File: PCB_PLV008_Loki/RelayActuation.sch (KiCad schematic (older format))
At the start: 27 parts, among them J27 Conn_01x02, J28 Conn_01x02, J29 Conn_01x02, J30 Conn_01x01, J31 Conn_01x01, J32 Conn_01x01, J33 Conn_01x01, J34 Conn_01x02, J35 Conn_01x02, J36 Conn_01x01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

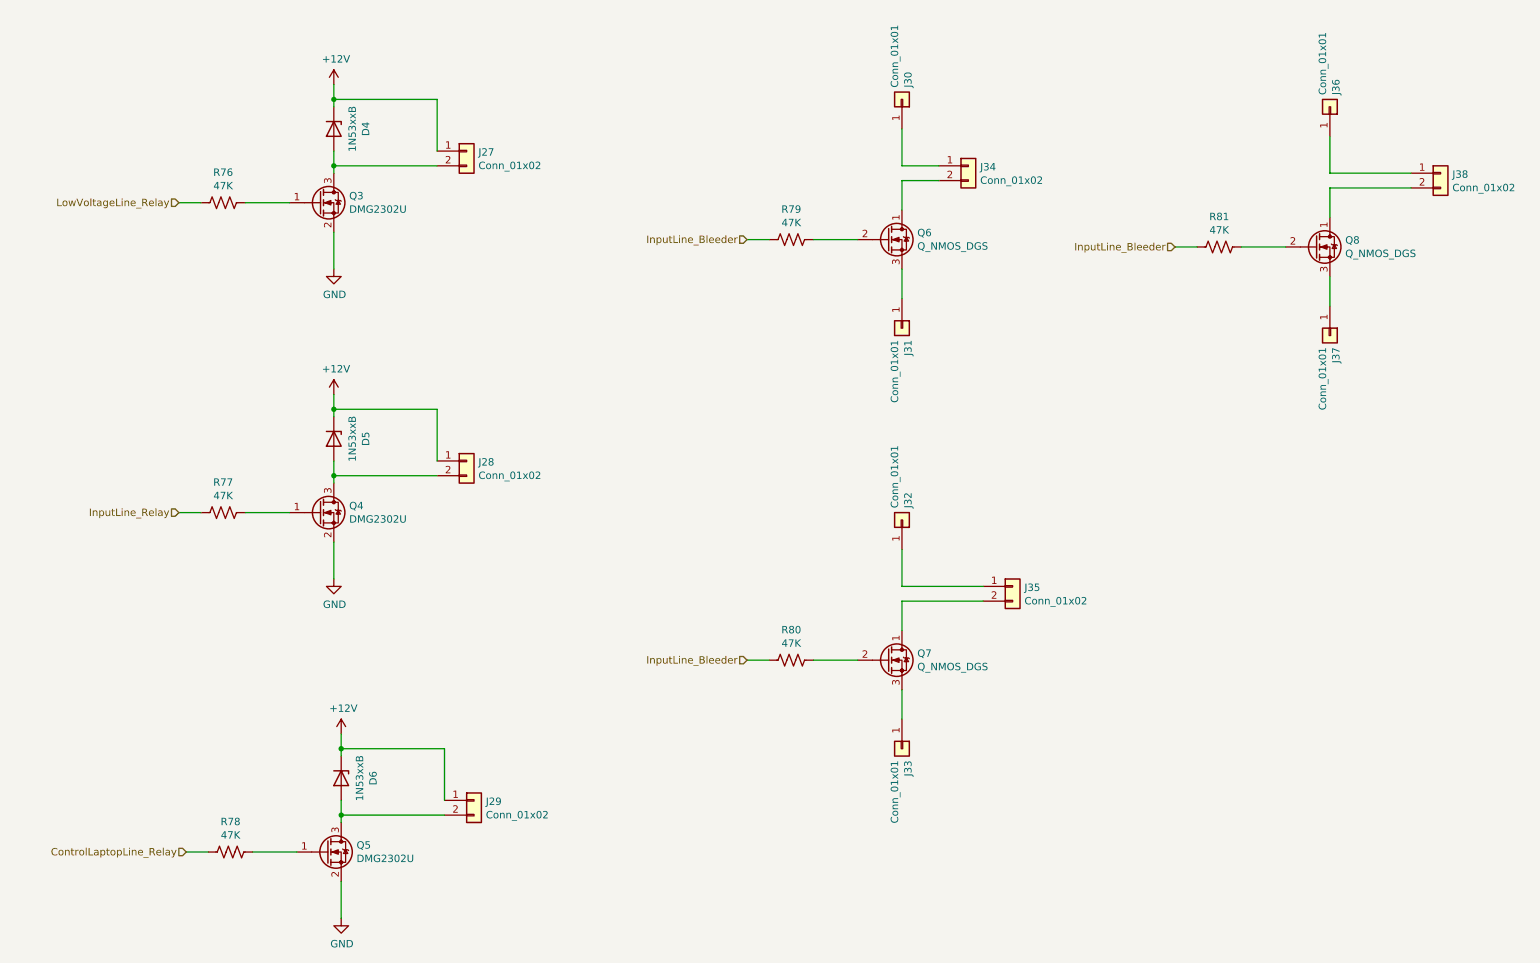
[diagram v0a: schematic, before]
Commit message: Schematic Clean up, Fan Actuation, SSR actuation sch fix
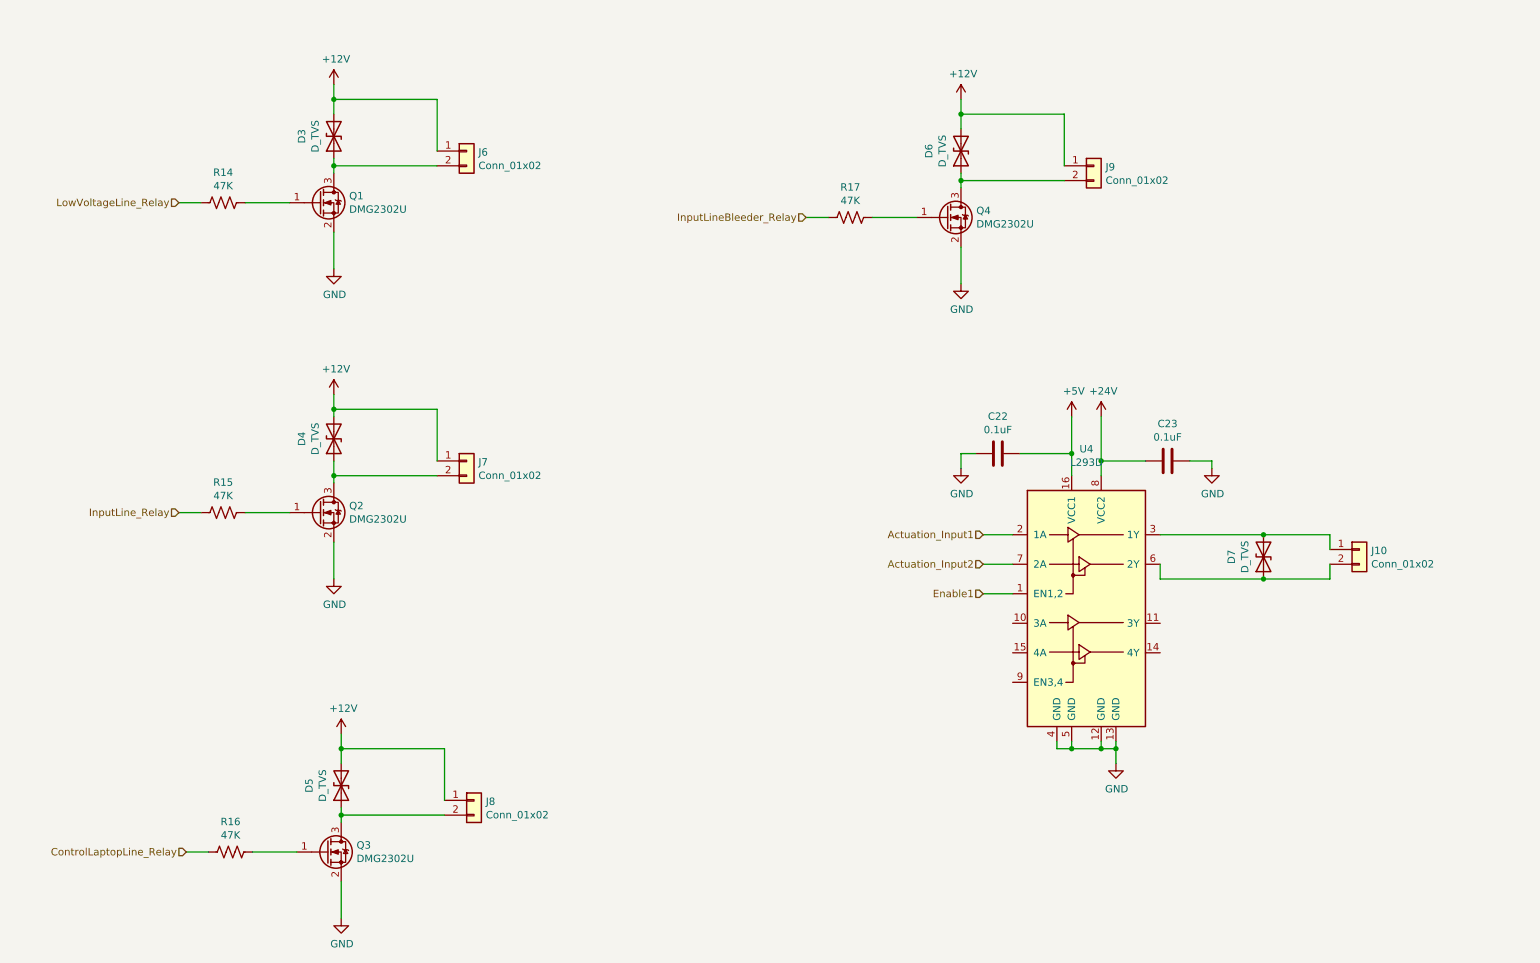
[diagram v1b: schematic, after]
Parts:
- removed D4, D5, D6: 1N53xxB, Diode_THT:D_DO-201_P15.24mm_Horizontal, symbol Diode:1N53xxB
- removed J30, J31, J32, J33, J36, J37: Conn_01x01, symbol Connector_Generic:Conn_01x01
- removed J34, J35, J38: Conn_01x02, symbol Connector_Generic:Conn_01x02
- removed Q6, Q7, Q8: Q_NMOS_DGS, symbol Device:Q_NMOS_DGS
- removed R79, R80, R81: 47K, symbol Device:R_US
- added C22, C23: 0.1uF, symbol Device:C
- added D3, D4, D5, D6, D7: D_TVS, symbol Device:D_TVS
- added J10: Conn_01x02, symbol Connector_Generic:Conn_01x02
- added J9: Conn_01x02, Connector_Molex:Molex_Micro-Fit_3.0_43650-0200_1x02_P3.00mm_Horizontal, symbol Connector_Generic:Conn_01x02
- added Q4: DMG2302U, Package_TO_SOT_SMD:SOT-23, symbol Transistor_FET:DMG2302U
- added R17: 47K, Resistor_SMD:R_0603_1608Metric_Pad0.98x0.95mm_HandSolder, symbol Device:R_US
- added U4: L293D, Package_DIP:DIP-16_W7.62mm, symbol Driver_Motor:L293D
- J6: renamed from J27; footprint (none) -> Connector_Molex:Molex_Micro-Fit_3.0_43650-0200_1x02_P3.00mm_Horizontal
- J7: renamed from J28; footprint (none) -> Connector_Molex:Molex_Micro-Fit_3.0_43650-0200_1x02_P3.00mm_Horizontal
- J8: renamed from J29; footprint (none) -> Connector_Molex:Molex_Micro-Fit_3.0_43650-0200_1x02_P3.00mm_Horizontal
- R14: renamed from R76; footprint (none) -> Resistor_SMD:R_0603_1608Metric_Pad0.98x0.95mm_HandSolder
- R15: renamed from R77; footprint (none) -> Resistor_SMD:R_0603_1608Metric_Pad0.98x0.95mm_HandSolder
- R16: renamed from R78; footprint (none) -> Resistor_SMD:R_0603_1608Metric_Pad0.98x0.95mm_HandSolder
- renumbered Q3 to Q1, Q4 to Q2, Q5 to Q3
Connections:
- net +12V: now also D3.2 (A2), D4.2 (A2), D5.2 (A2), D6.2 (A2), J9.1 (Pin_1)
- net GND: now also C22.1, C23.2, Q4.2 (S), U4.12 (GND), U4.13 (GND), U4.4 (GND), U4.5 (GND)
- net at J6.2 (Pin_2), Q1.3 (D): now also D3.1 (A1)
- net at J8.2 (Pin_2), Q3.3 (D): now also D5.1 (A1)
- net at J7.2 (Pin_2), Q2.3 (D): now also D4.1 (A1)
- new net: Q4.1 (G), R17.2
- new net: D6.1 (A1), J9.2 (Pin_2), Q4.3 (D)
- new net: D7.2 (A2), J10.1 (Pin_1), U4.3 (1Y)
- new net: D7.1 (A1), J10.2 (Pin_2), U4.6 (2Y)
- new net +24V: C23.1, U4.8 (VCC2)
- new net +5V: C22.2, U4.16 (VCC1)
- new net Actuation_Input1: U4.2 (1A)
- new net Actuation_Input2: U4.7 (2A)
- new net Enable1: U4.1 (EN1,2)
- new net InputLineBleeder_Relay: R17.1
